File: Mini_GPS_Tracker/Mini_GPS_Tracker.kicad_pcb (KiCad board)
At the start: 4 copper layers, 38.1 x 105.4 mm, 62 parts, among them J1 USB_C_Receptacle, J2 Screw_Terminal_01x02, J3 901-10512-1, J4 Conn_ARM_JTAG_SWD_10, SW1 SW_Push, SW2 MLL1200S, U1 FT230XS, U10 ADXL343, U11 BNO055, U2 MS5611-01BA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

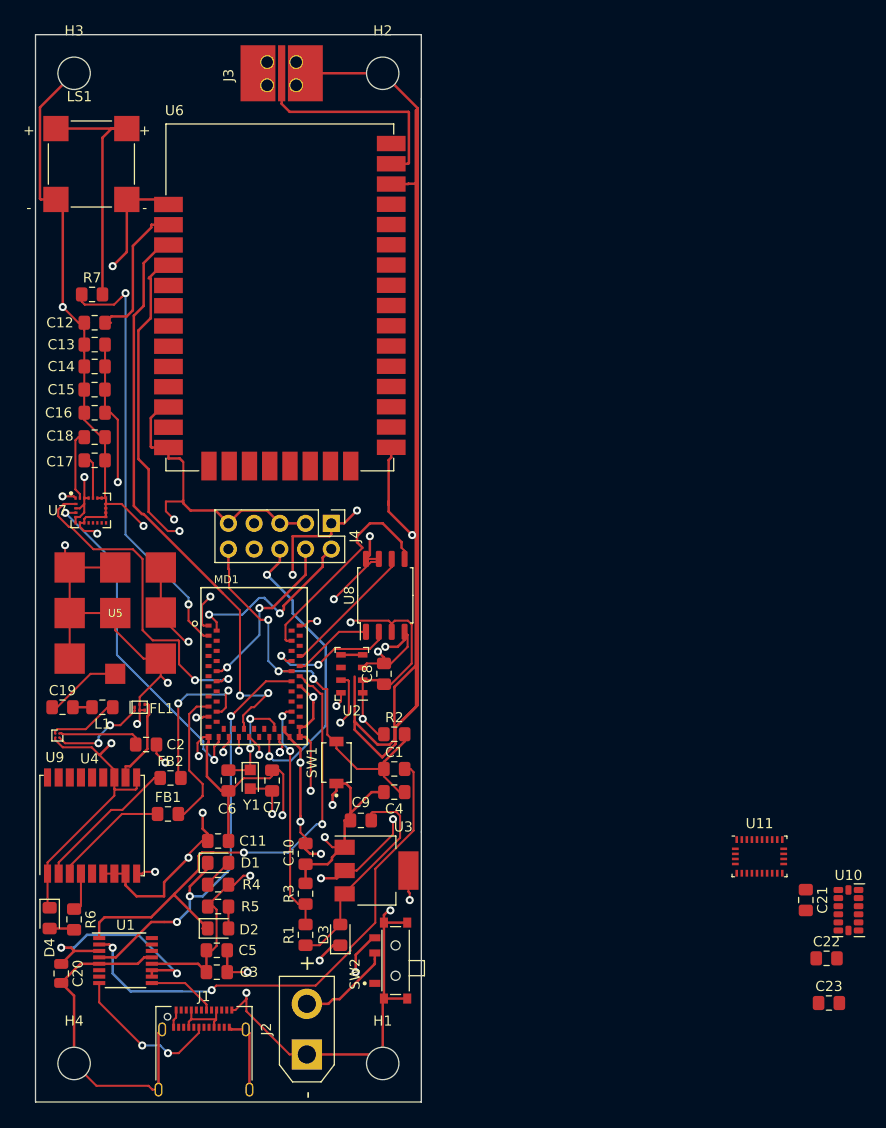
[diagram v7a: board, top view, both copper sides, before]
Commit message: added stm chip
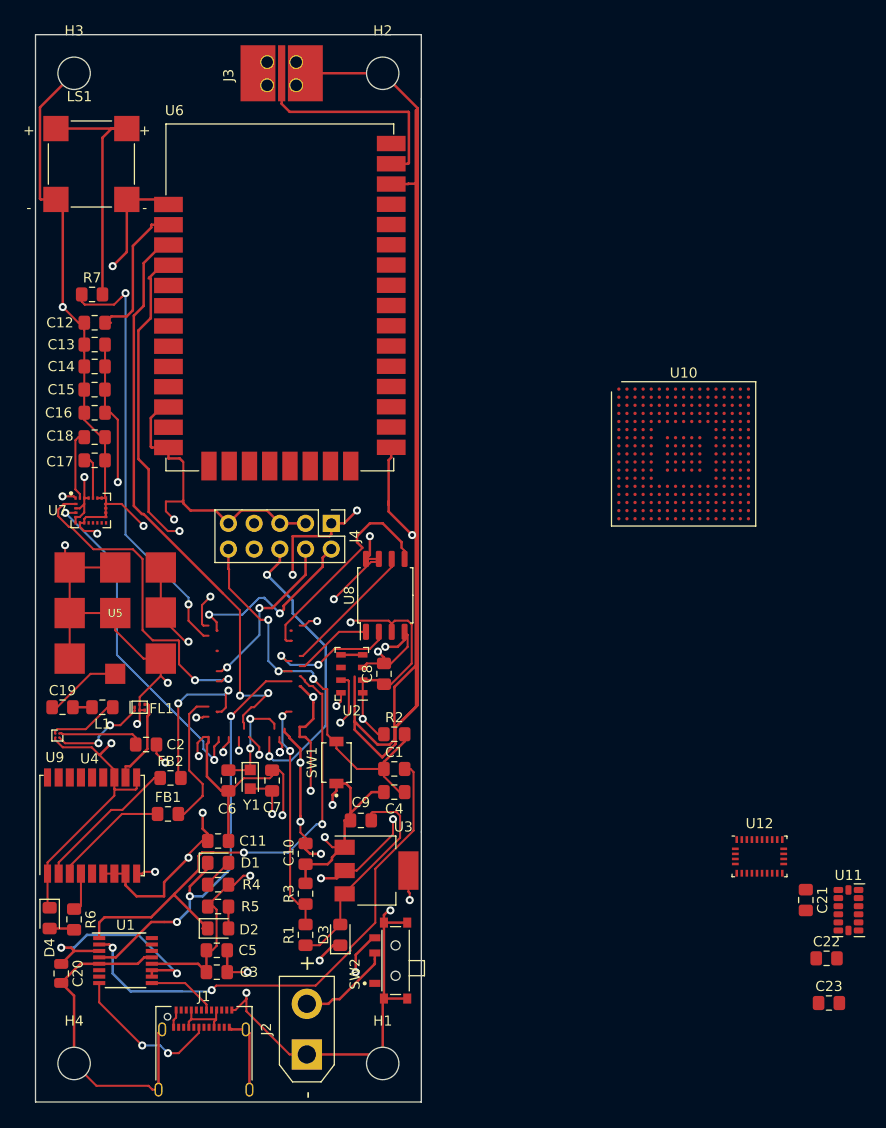
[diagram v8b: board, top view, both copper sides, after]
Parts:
- removed MD1: SPARKFUN_WRL-15376, Sparkfun-Artemis:SPARKFUN_WRL-15376
- added U10: STMICROELECTRONICS_STM32H747XIH6, Package_BGA:TFBGA-265_14x14mm_Layout17x17_P0.8mm, F.Cu at (211.3, 75.7)
- renumbered U10 to U11, U11 to U12
